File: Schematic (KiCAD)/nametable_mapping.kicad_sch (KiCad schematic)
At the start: 40 parts

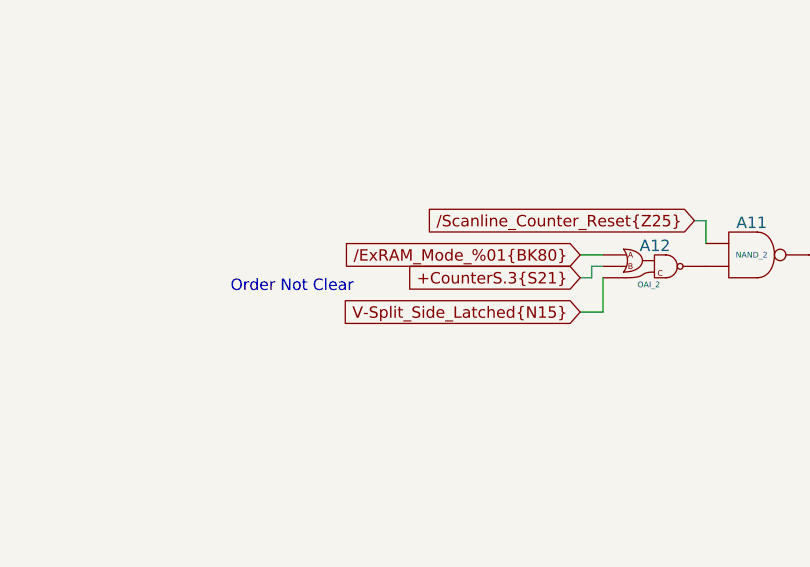
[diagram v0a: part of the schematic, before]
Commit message: - Lots of additional comments and signal name improvements.  - "Don't know what this is yet but it is important" section of the pulse channels:    - I worked out the logic and it is a 4-bit binary up-counter with preload, made from gates and D-latches instead of T-flip-flops.    - It is extremely similar to the envelope counter, but takes twice the die space and much more traces.    - None of its outputs go anywhere else, so I believe that it has no actual function.    - It seems to be a previous attempt at making the envelope counter and it got disconnected and left in.    - Each pulse channel has its own copy and I moved both of them to the "Artifacts" sheet.    - The wasted space amounts to about half of one of the large columns on the left side of the die.  - A couple of "OAI2" cells that noted "unclear order": I determined the correct order of the inputs based on several others which were known.  - Deduced the purpose of the 2 separate methods of scanline detection:    - The one looking for 3 consecutive reads finds the start of a scanline.    - The one counting PPU /RD to find PPU cycle 336, finds the end of the scanline.    - I moved these beside each other on the same sheet for clarity.  - A66.5 Changed from Nand to Nor in order to make sense.  - Basic test mode:    - Pin 92: Active low, enables test mode.    - Pin 29: In test mode, it gives external control of "Scanline Start Detection", which is normally done with the familiar 3 matching PPU reads.  When not in test mode, the pin has no function.    - Pin 30: In test mode, it gives external control of "Scanline End Detection", which is normally done by counting PPU /RD to find PPU cycle 336.  It also gives control of "Pulse Length Clock" when in test mode.  When not in test mode, the pin has no function.    - Pin 98/SL3: In test mode, it gives external control of "Pulse Timer Clock".  Whether or not in test mode, this pin low makes the MMC5 pretend $5104 had not yet been written since reset, probably as a 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
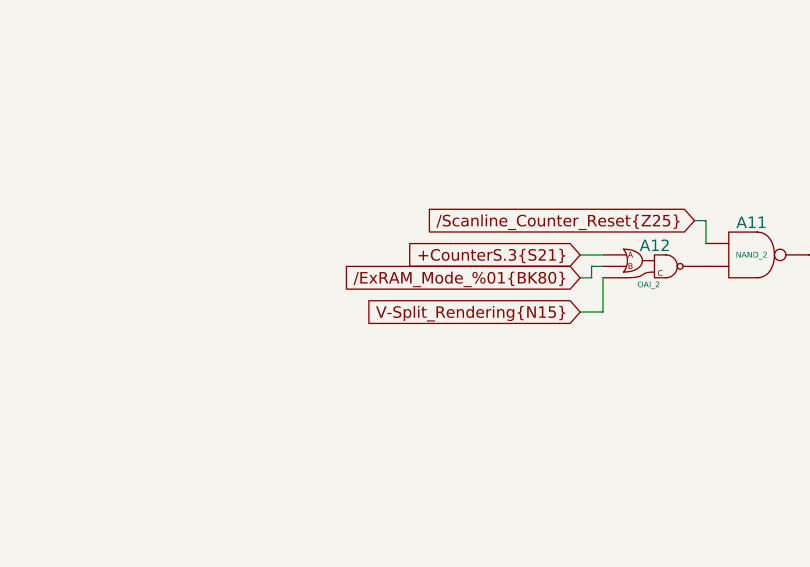
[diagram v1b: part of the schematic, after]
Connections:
- net V-Split_Side_Latched{N15} is gone; now on net /ExRAM_Mode_%01{BK80}: A12. (X)
- new net: B9. (X), C1. (/Q7)
- new net: A13. (X), A14. (X), B18. (X), B19. (X), B20. (X), B21. (X), B22. (X), B23. (X), B24. (X), B25. (X)
- new net: A9. (Y4), B25. (X)
- new net: B6. (X), C1. (/Q7)
- new net: A9. (Y4), B23. (X)
- new net: A16. (X), B14. (X), B15. (X), B16. (X), B17. (X)
- new net: A13. (X), B14. (X), B15. (X), B16. (X), B17. (X)
- new net: A9. (Y4), B16. (X)
- new net: B10. (X), C1. (/Q7)
- new net: A9. (Y4), B15. (X)
- new net: B7. (X), C1. (/Q7)
- new net: A11. (X), A12. (X)
- new net: A10. (X), A11. (X)
- new net: B4. (X), C1. (/Q7)
- new net: BL11. (X), BL33. (X)
- new net: B11. (X), C1. (/Q7)
- new net: B3. (X), C1. (/Q7)
- new net: A9. (Y4), B22. (X)
- new net: A17. (X), C1. (/Q7)
- new net: A9. (Y4), B14. (X)
- new net: A9. (Y4), B21. (X)
- new net: A9. (Y4), B18. (X)
- new net: A9. (Y4), B20. (X)
- new net: A9. (Y4), B19. (X)
- new net: A9. (Y4), B17. (X)
- new net: A9. (Y4), B24. (X)
- new net: B13. (X), C1. (/Q7)
- new net: B12. (X), C1. (/Q7)
- new net: B5. (X), C1. (/Q7)
- new net: B8. (X), C1. (/Q7)
- new net V-Split_Rendering{N15}: A12. (X)
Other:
- note removed: "Order Not Clear"
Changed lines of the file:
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@@
 	(generator_version "9.0")
 	(paper "USLedger")
-	(text "Order Not Clear"
-		(exclude_from_sim no)
-		(at 79.756 68.326 0)
-		(effects
-			(font
-				(size 1.27 1.27)
-			)
-		)
-	)
 	(text "I believe this uses\ninverting tristate buffers."
 		(exclude_from_sim no)
@@
 	(wire
 		(pts
+			(xy 111.76 67.31) (xy 113.03 67.31)
+		)
+		(stroke
+			(width 0)
+			(type default)
+		)
+	)
+	(wire
+		(pts
 			(xy 195.58 154.94) (xy 201.93 154.94)
 		)
@@
 	(wire
 		(pts
-			(xy 113.03 66.04) (xy 114.3 66.04)
-		)
-		(stroke
-			(width 0)
-			(type default)
-		)
-	)
-	(wire
-		(pts
 			(xy 223.52 114.3) (xy 196.85 114.3)
 		)
@@
 	(wire
 		(pts
+			(xy 111.76 71.12) (xy 114.3 71.12)
+		)
+		(stroke
+			(width 0)
+			(type default)
+		)
+	)
+	(wire
+		(pts
 			(xy 80.01 173.99) (xy 95.25 173.99)
 		)
@@
 	(wire
 		(pts
-			(xy 111.76 71.12) (xy 114.3 71.12)
-		)
-		(stroke
-			(width 0)
-			(type default)
-		)
-	)
-	(wire
-		(pts
 			(xy 96.52 143.51) (xy 104.14 143.51)
 		)
@@
 	(wire
 		(pts
-			(xy 111.76 67.31) (xy 113.03 67.31)
-		)
-		(stroke
-			(width 0)
-			(type default)
-		)
-	)
-	(wire
-		(pts
 			(xy 223.52 83.82) (xy 223.52 29.21)
 		)
@@
 	(wire
 		(pts
+			(xy 113.03 66.04) (xy 113.03 67.31)
+		)
+		(stroke
+			(width 0)
+			(type default)
+		)
+	)
+	(wire
+		(pts
 			(xy 166.37 64.77) (xy 166.37 73.66)
 		)
@@
 	(wire
 		(pts
-			(xy 113.03 67.31) (xy 113.03 66.04)
-		)
-		(stroke
-			(width 0)
-			(type default)
-		)
-	)
-	(wire
-		(pts
 			(xy 236.22 125.73) (xy 236.22 132.08)
 		)
@@
 	(wire
 		(pts
+			(xy 114.3 71.12) (xy 114.3 67.31)
+		)
+		(stroke
+			(width 0)
+			(type default)
+		)
+	)
+	(wire
+		(pts
+			(xy 114.3 66.04) (xy 113.03 66.04)
+		)
+		(stroke
+			(width 0)
+			(type default)
+		)
+	)
+	(wire
+		(pts
 			(xy 163.83 85.09) (xy 163.83 93.98)
 		)
@@
 		(pts
 			(xy 194.31 49.53) (xy 193.04 49.53)
-		)
-		(stroke
-			(width 0)
-			(type default)
-		)
-	)
-	(wire
-		(pts
-			(xy 114.3 71.12) (xy 114.3 67.31)
 		)
 		(stroke
@@
 	(global_label "+CounterS.3{S21}"
 		(shape input)
-		(at 111.76 67.31 180)
-		(fields_autoplaced yes)
-		(effects
-			(font
-				(size 1.27 1.27)
-			)
-			(justify right)
-		)
-		(property "Intersheetrefs" "${INTERSHEET_REFS}"
-			(at 91.5392 67.31 0)
+		(at 111.76 64.77 180)
+		(fields_autoplaced yes)
+		(effects
+			(font
+				(size 1.27 1.27)
+			)
+			(justify right)
+		)
+		(property "Intersheetrefs" "${INTERSHEET_REFS}"
+			(at 91.5392 64.77 0)
 			(effects
 				(font
@@
 		)
 	)
-	(global_label "V-Split_Side_Latched{N15}"
+	(global_label "V-Split_Rendering{N15}"
 		(shape input)
 		(at 111.76 71.12 180)
@@
 		)
 		(property "Intersheetrefs" "${INTERSHEET_REFS}"
-			(at 82.9516 71.12 0)
+			(at 85.9149 71.12 0)
 			(effects
 				(font
@@
 	(global_label "{slash}ExRAM_Mode_%01{BK80}"
 		(shape input)
-		(at 111.76 64.77 180)
-		(fields_autoplaced yes)
-		(effects
-			(font
-				(size 1.27 1.27)
-			)
-			(justify right)
-		)
-		(property "Intersheetrefs" "${INTERSHEET_REFS}"
-			(at 84.1612 64.77 0)
-			(effects
-				(font
+		(at 111.76 67.31 180)
+		(fields_autoplaced yes)
+		(effects
+			(font
+				(size 1.27 1.27)
+			)
+			(justify right)
+		)
+		(property "Intersheetrefs" "${INTERSHEET_REFS}"
+			(at 84.1612 67.31 0)
+			(effects
+				(font

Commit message: Schematic and SVG Updates
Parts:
- added S1: BUFFER, symbol MMC5:BUFFER
- added S2: NAND_2, symbol MMC5:NAND_2
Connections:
- net +CounterS.3{S21} is gone; now on net /ExRAM_Mode_%01{BK80}: A12. (X)
- new net: B9. (X), C1. (/Q7)
- new net: A13. (X), A14. (X), B18. (X), B19. (X), B20. (X), B21. (X), B22. (X), B23. (X), B24. (X), B25. (X)
- new net: A9. (Y4), B25. (X)
- new net: B6. (X), C1. (/Q7)
- new net: A9. (Y4), B23. (X)
- new net: A16. (X), B14. (X), B15. (X), B16. (X), B17. (X)
- new net: A13. (X), B14. (X), B15. (X), B16. (X), B17. (X)
- new net: A9. (Y4), B16. (X)
- new net: S1. (X), S2. (X)
- new net: B10. (X), C1. (/Q7)
- new net: A9. (Y4), B15. (X)
- new net: B7. (X), C1. (/Q7)
- new net: A11. (X), A12. (X)
- new net: A10. (X), A11. (X)
- new net: B4. (X), C1. (/Q7)
- new net: BL11. (X), BL33. (X)
- new net: B11. (X), C1. (/Q7)
- new net: A12. (X), S1. (X)
- new net: B3. (X), C1. (/Q7)
- new net: A9. (Y4), B22. (X)
- new net: A17. (X), C1. (/Q7)
- new net: A9. (Y4), B14. (X)
- new net: A9. (Y4), B21. (X)
- new net: A9. (Y4), B18. (X)
- new net: A9. (Y4), B20. (X)
- new net: A9. (Y4), B19. (X)
- new net: A9. (Y4), B17. (X)
- new net: A9. (Y4), B24. (X)
- new net: B13. (X), C1. (/Q7)
- new net: B12. (X), C1. (/Q7)
- new net: B5. (X), C1. (/Q7)
- new net: B8. (X), C1. (/Q7)
- new net +PPU_Fetch_Count.0{S10}: S2. (X)
- new net +PPU_Fetch_Count.1{S13}: S2. (X)
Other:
- note added: "Low for every 4th PPU Fetch"
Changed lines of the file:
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@@
 		)
 	)
+	(text "Low for every\n4th PPU Fetch"
+		(exclude_from_sim no)
+		(at 90.17 58.166 0)
+		(effects
+			(font
+				(size 1.27 1.27)
+			)
+			(justify right)
+		)
+	)
 	(text "Note: There is probably\nan inverter at each \noutput pin."
 		(exclude_from_sim no)
@@
 	(wire
 		(pts
-			(xy 111.76 67.31) (xy 113.03 67.31)
+			(xy 111.76 69.85) (xy 113.03 69.85)
 		)
 		(stroke
@@
 	(wire
 		(pts
-			(xy 111.76 64.77) (xy 114.3 64.77)
+			(xy 87.63 143.51) (xy 80.01 143.51)
 		)
 		(stroke
@@
 	(wire
 		(pts
-			(xy 87.63 143.51) (xy 80.01 143.51)
+			(xy 163.83 76.2) (xy 163.83 85.09)
 		)
 		(stroke
@@
 	(wire
 		(pts
-			(xy 163.83 76.2) (xy 163.83 85.09)
+			(xy 165.1 166.37) (xy 165.1 175.26)
 		)
 		(stroke
@@
 	(wire
 		(pts
-			(xy 165.1 166.37) (xy 165.1 175.26)
+			(xy 223.52 114.3) (xy 196.85 114.3)
 		)
 		(stroke
@@
 	(wire
 		(pts
-			(xy 223.52 114.3) (xy 196.85 114.3)
+			(xy 195.58 116.84) (xy 223.52 116.84)
 		)
 		(stroke
@@
 	(wire
 		(pts
-			(xy 195.58 116.84) (xy 223.52 116.84)
+			(xy 165.1 157.48) (xy 184.15 157.48)
 		)
 		(stroke
@@
 	(wire
 		(pts
-			(xy 165.1 157.48) (xy 184.15 157.48)
+			(xy 93.98 64.77) (xy 114.3 64.77)
 		)
 		(stroke
@@
 	(wire
 		(pts
-			(xy 125.73 60.96) (xy 125.73 63.5)
+			(xy 125.73 59.69) (xy 125.73 63.5)
 		)
 		(stroke
@@
 	(wire
 		(pts
-			(xy 111.76 71.12) (xy 114.3 71.12)
+			(xy 111.76 73.66) (xy 114.3 73.66)
 		)
 		(stroke
@@
 	(wire
 		(pts
-			(xy 113.03 66.04) (xy 113.03 67.31)
+			(xy 113.03 66.04) (xy 113.03 69.85)
 		)
 		(stroke
@@
 	(wire
 		(pts
-			(xy 114.3 71.12) (xy 114.3 67.31)
+			(xy 114.3 73.66) (xy 114.3 67.31)
 		)
 		(stroke
@@
 	(wire
 		(pts
-			(xy 124.46 60.96) (xy 125.73 60.96)
+			(xy 124.46 59.69) (xy 125.73 59.69)
 		)
 		(stroke
@@
 	(global_label "{slash}Scanline_Counter_Reset{Z25}"
 		(shape input)
-		(at 124.46 60.96 180)
+		(at 124.46 59.69 180)
 		(fields_autoplaced yes)
 		(effects
@@
 		)
 		(property "Intersheetrefs" "${INTERSHEET_REFS}"
-			(at 92.265 60.96 0)
+			(at 92.265 59.69 0)
 			(effects
 				(font
@@
 		)
 	)
-	(global_label "+CounterS.3{S21}"
-		(shape input)
-		(at 111.76 64.77 180)
-		(fields_autoplaced yes)
-		(effects
-			(font
-				(size 1.27 1.27)
-			)
-			(justify right)
-		)
-		(property "Intersheetrefs" "${INTERSHEET_REFS}"
-			(at 91.5392 64.77 0)
-			(effects
-				(font
-					(size 1.27 1.27)
-				)
-				(justify right)
-				(hide yes)
-			)
-		)
-	)
 	(global_label "+$5105.0{B3}"
 		(shape output)
@@
 		)
 	)
+	(global_label "+PPU_Fetch_Count.0{S10}"
+		(shape input)
+		(at 73.66 66.04 180)
+		(fields_autoplaced yes)
+		(effects
+			(font
+				(size 1.27 1.27)
+			)
+			(justify right)
+		)
+		(property "Intersheetrefs" "${INTERSHEET_REFS}"
+			(at 45.5773 66.04 0)
+			(effects
+				(font
+					(size 1.27 1.27)
+				)
+				(justify right)
+				(hide yes)
+			)
+		)
+	)
 	(global_label "CIRAM_CE_PIN{A9}"
 		(shape output)
@@
 	(global_label "V-Split_Rendering{N15}"
 		(shape input)
-		(at 111.76 71.12 180)
+		(at 111.76 73.66 180)
 		(fields_autoplaced yes)
 		(effects
@@
 		)
 		(property "Intersheetrefs" "${INTERSHEET_REFS}"
-			(at 85.9149 71.12 0)
+			(at 85.9149 73.66 0)
 			(effects
 				(font
@@
 		)
 	)
+	(global_label "+PPU_Fetch_Count.1{S13}"
+		(shape input)
+		(at 73.66 63.5 180)
+		(fields_autoplaced yes)
+		(effects
+			(font
+				(size 1.27 1.27)
+			)
+			(justify right)
+		)
+		(property "Intersheetrefs" "${INTERSHEET_REFS}"
+			(at 45.5773 63.5 0)
+			(effects
+				(font
+					(size 1.27 1.27)
+				)
+				(justify right)
+				(hide yes)
+			)
+		)
+	)
 	(global_label "+$5105.6{A17}"
 		(shape output)
@@
 	(global_label "{slash}ExRAM_Mode_%01{BK80}"
 		(shape input)
-		(at 111.76 67.31 180)
+		(at 111.76 69.85 180)
 		(fields_autoplaced yes)
 		(effects
@@
 		)
 		(property "Intersheetrefs" "${INTERSHEET_REFS}"
-			(at 84.1612 67.31 0)
+			(at 84.1612 69.85 0)
 			(effects
 				(font
@@
 	)
 	(symbol
+		(lib_name "NAND_2_45")
+		(lib_id "MMC5:NAND_2")
+		(at 78.74 64.77 0)
+		(unit 1)
+		(exclude_from_sim no)
+		(in_bom yes)
+		(on_board yes)
+		(dnp no)
+		(fields_autoplaced yes)
+		(property "Reference" "S2"
+			(at 78.74 60.452 0)
+			(do_not_autoplace yes)
+			(effects
+				(font
+					(size 1.27 1.27)
+				)
+				(justify top)
+			)
+		)
+		(property "Value" "NAND_2"
+			(at 78.74 64.77 0)
+			(do_not_autoplace yes)
+			(effects
+				(font
+					(size 0.635 0.635)
+				)
+			)
+		)
+		(property "Footprint" ""
+			(at 78.74 64.77 0)
+			(effects
+				(font
+					(size 1.27 1.27)
+				)
+				(hide yes)
+			)
+		)
+		(property "Datasheet" ""
+			(at 78.74 64.77 0)
+			(effects
+				(font
+					(size 1.27 1.27)
+				)
+				(hide yes)
+			)
+		)
+		(property "Description" ""
+			(at 78.74 64.77 0)
+			(effects
+				(font
+					(size 1.27 1.27)
+				)
+				(hide yes)
+			)
+		)
+		(pin ""
+		)
+		(pin ""
+		)
+		(pin ""
+		)
+		(instances
+			(project "MMC5"
+				(path "/46093bf6-f83e-4237-9ece-7350a682aff0/d931b895-16b8-4266-a6e9-dc595d1a00c0"
+					(reference "S2")
+					(unit 1)
+				)
+			)
+		)
+	)
+	(symbol
 		(lib_name "NAND_2_3")
 		(lib_id "MMC5:NAND_2")
@@
 					(unit 1)
 				)
+			)
+		)
+	)
+	(symbol
+		(lib_name "BUFFER_29")
+		(lib_id "MMC5:BUFFER")
+		(at 88.9 64.77 0)
+		(unit 1)
+		(exclude_from_sim no)
+		(in_bom yes)
+		(on_board yes)
+		(dnp no)
+		(fields_autoplaced yes)
+		(property "Reference" "S1"
+			(at 88.9 61.468 0)
+			(do_not_autoplace yes)
+			(effects
+				(font
+					(size 1.27 1.27)
+				)
+				(justify top)
+			)
+		)
+		(property "Value" "BUFFER"
+			(at 91.694 66.04 0)
+			(do_not_autoplace yes)
+			(effects
+				(font
+					(size 0.635 0.635)
+				)
+			)
+		)
+		(property "Footprint" ""
+			(at 88.9 64.77 0)
+			(effects
+				(font
+					(size 1.27 1.27)
+				)
+				(hide yes)
+			)
+		)
+		(property "Datasheet" ""
+			(at 88.9 64.77 0)
+			(effects
+				(font
+					(size 1.27 1.27)
+				)
+				(hide yes)
+			)
+		)
+		(property "Description" ""
+			(at 88.9 64.77 0)
+			(effects
+				(font
+					(size 1.27 1.27)
+				)
+				(hide yes)
+			)
+		)
+		(pin ""
+		)
+		(pin ""
+		)
+		(instances
+			(project "MMC5"
+				(path "/46093bf6-f83e-4237-9ece-7350a682aff0/d931b895-16b8-4266-a6e9-dc595d1a00c0"
+					(reference "S1")
+					(unit 1)
+				)
